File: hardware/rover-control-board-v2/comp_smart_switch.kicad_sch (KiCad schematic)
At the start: 26 parts, among them Q3 Q_NMOS_DGS, Q4 Q_PMOS_DGS, U2 BTH50015

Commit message: progress
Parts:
- added D12: RED, symbol Device:LED
- added J11: EXT_TEMP_PROBE, symbol Connector_Generic:Conn_01x02
- added Q2: Q_NMOS, symbol Device:Q_NMOS
- added R22, R24: 10k, symbol Device:R
- added R23: 100R, symbol Device:R
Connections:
- net GND: now also Q2.S, R24.2
- net 3V3: now reaches JP2.1 (A)
- net 3V3: now also JP1.1 (A), U1.2 (VCC), D12.2 (A)
- net TEMP_INT_: now reaches U1.11 (INT_)
- net SDATA: now reaches U1.12 (SDATA)
- net SCLK: now reaches U1.14 (SCLK)
- net TEMP_ALARM_: now reaches U1.16 (T_ALARM)
- net TEMP_ALARM_: now also R23.2
- net at U1.3 (D+): now also J11.2 (Pin_2)
- net at U1.4 (D-): now also J11.1 (Pin_1)
- new net: D12.1 (K), R22.2
- new net: Q2.D, R22.1
- new net: Q2.G, R23.1, R24.1
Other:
- note added: "1x02 pin header"
- note added: "OVER TEMP"
- note added: "Use 2N3906 for external temp probe"
- moved on the sheet: JP1, JP2

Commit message: Channels routed, temp bus pending
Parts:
- added C50: 100nF, symbol Device:C
- added D11, D13: ESD5Zxx, Diode_SMD:D_SOD-523, symbol Diode:ESD5Zxx
- J11: value EXT_TEMP_PROBE -> TEMP_PROBE
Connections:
- net 3V3: now also C50.2
- net GND: now also C50.1, D11.2 (A), D13.2 (A)
- net V_sense: now also D13.1 (K)
- net i_sense: now also D11.1 (K)
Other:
- note added: "5v varient needed"
- note removed: "Add TVS"
- note removed: "Add TVS or Opto Coupler"

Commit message: Bus routed
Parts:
- renumbered C50 to C16, C6 to C17, C2 to C18, C3 to C19, C4 to C20, C5 to C21, D3 to D5, D12 to D6, D11 to D7, D2 to D8, D13 to D9, J11 to J10, Q2 to Q5, R7 to R14, R5 to R15, R6 to R16, R2 to R18, R3 to R19, R4 to R20, R22 to R21, R23 to R22, R24 to R23, R8 to R24, R9 to R25, R11 to R26, R10 to R27, R12 to R28, R13 to R29, U1 to U5, U2 to U6

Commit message: revamping channel switches
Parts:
- renumbered C16 to C10, C17 to C11, C18 to C12, C19 to C13, C20 to C14, C21 to C15, J10 to J11, R14 to R13, R15 to R14, R16 to R15, R17 to R16, R18 to R17, R19 to R18, R20 to R19, R21 to R20, R22 to R21, R23 to R22, R24 to R23, R25 to R24, R26 to R25, R27 to R26, R28 to R27, R29 to R28, U5 to U4, U6 to U5
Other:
- moved on the sheet: C11, C12, C13, C14, C15, D7, D8, D9, R23, R24, R25, R26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

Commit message: 10v reg added for charge pumps
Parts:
- added Q25: CSD19533Q5A, Package_TO_SOT_SMD:TDSON-8-1, symbol Transistor_FET:CSD19533Q5A
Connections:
- new net: Q25.1 (S), Q25.2 (S), Q25.3 (S)
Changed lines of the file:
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@@
+	)
+	(symbol
+		(lib_id "Transistor_FET:CSD19533Q5A")
+		(at 149.86 106.68 0)
+		(unit 1)
+		(body_style 1)
+		(exclude_from_sim no)
+		(in_bom yes)
+		(on_board yes)
+		(in_pos_files yes)
+		(dnp no)
+		(fields_autoplaced yes)
+		(property "Reference" "Q25"
+			(at 156.21 105.4099 0)
+			(show_name no)
+			(do_not_autoplace no)
+			(effects
+				(font
+					(size 1.27 1.27)
+				)
+				(justify left)
+			)
+		)
+		(property "Value" "CSD19533Q5A"
+			(at 156.21 107.9499 0)
+			(show_name no)
+			(do_not_autoplace no)
+			(effects
+				(font
+					(size 1.27 1.27)
+				)
+				(justify left)
+			)
+		)
+		(property "Footprint" "Package_TO_SOT_SMD:TDSON-8-1"
+			(at 154.94 108.585 0)
+			(hide yes)
+			(show_name no)
+			(do_not_autoplace no)
+			(effects
+				(font
+					(size 1.27 1.27)
+					(italic yes)
+				)
+				(justify left)
+			)
+		)
+		(property "Datasheet" "http://www.ti.com/lit/gpn/csd19533q5a"
+			(at 154.94 110.49 0)
+			(hide yes)
+			(show_name no)
+			(do_not_autoplace no)
+			(effects
+				(font
+					(size 1.27 1.27)
+				)
+				(justify left)
+			)
+		)
+		(property "Description" "100A Id, 100V Vds, NexFET N-Channel Power MOSFET, 9.5mOhm Ron, 27nC Qg(typ), SON8 5x6mm"
+			(at 149.86 106.68 0)
+			(hide yes)
+			(show_name no)
+			(do_not_autoplace no)
+			(effects
+				(font
+					(size 1.27 1.27)
+				)
+			)
+		)
+		(pin "2"
+		)
+		(pin "4"
+		)
+		(pin "3"
+		)
+		(pin "1"
+		)
+		(pin "5"
+		)
+		(instances
+			(project "rover-control-board-v2"
+				(path "/ed12625f-743c-4dd1-a6f4-666aeca01e2d/977b49b6-52fe-4534-aa9a-ea79bcc5d2a2"
+					(reference "Q25")
+					(unit 1)
+				)
+			)
+		)
 	)
 	(symbol

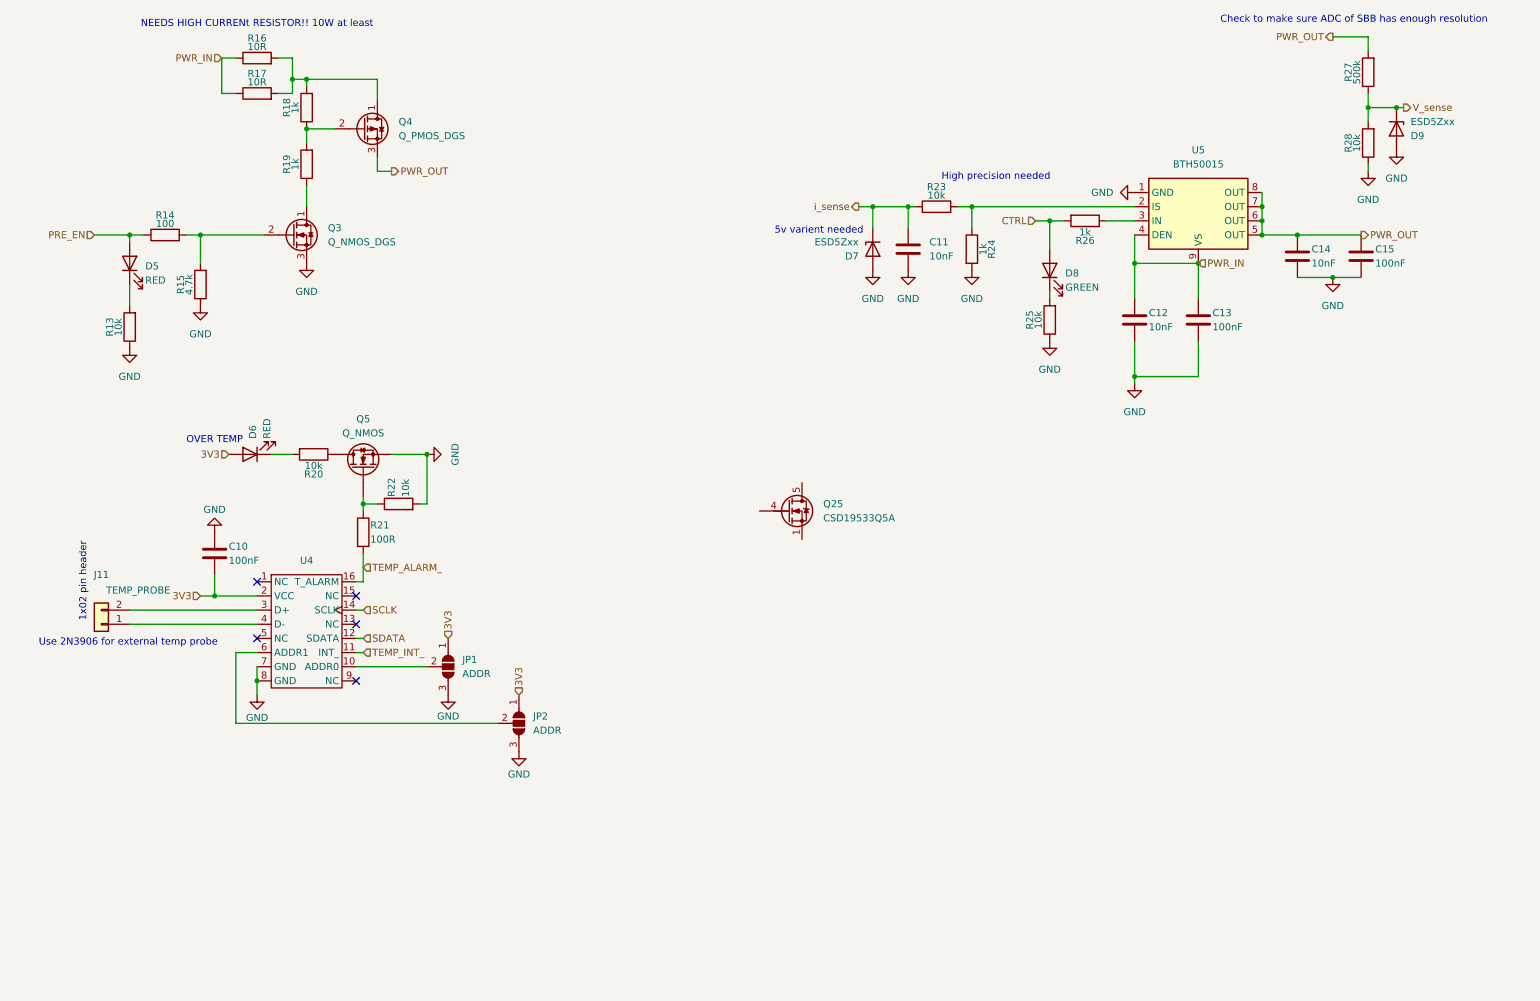
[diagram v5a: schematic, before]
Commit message: high power switch added
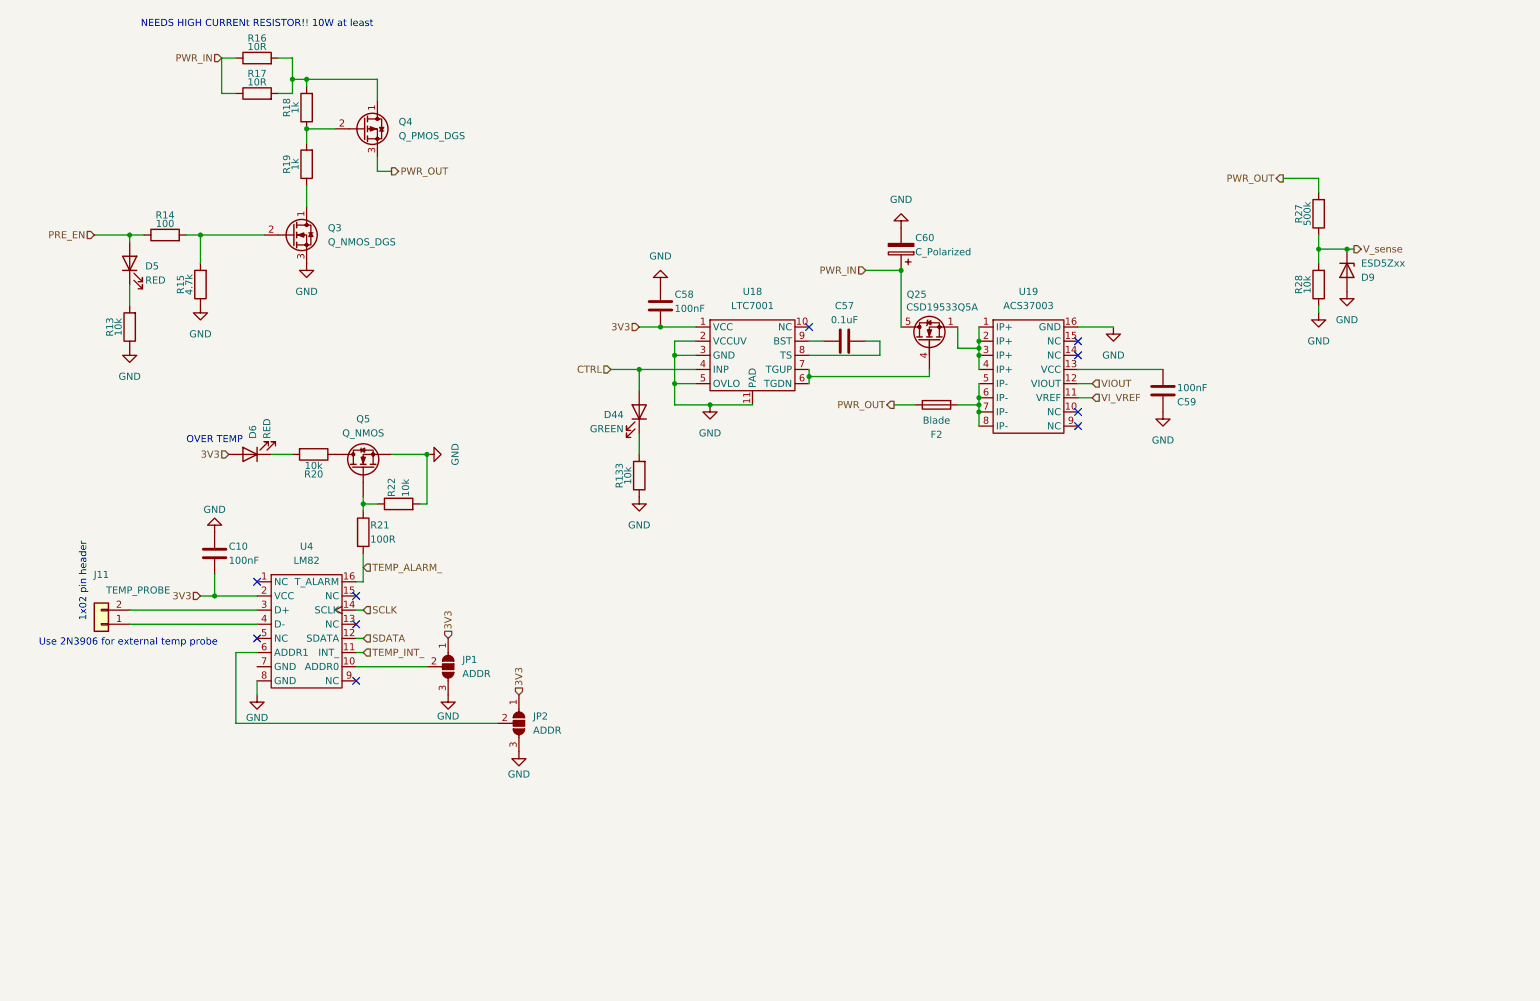
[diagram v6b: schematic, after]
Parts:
- removed C11, C12, C14: 10nF, symbol Device:C
- removed C13, C15: 100nF, symbol Device:C
- removed D7: ESD5Zxx, Diode_SMD:D_SOD-523, symbol Diode:ESD5Zxx
- removed D8: GREEN, symbol Device:LED
- removed R23, R25: 10k, symbol Device:R
- removed R24, R26: 1k, symbol Device:R
- removed U5: BTH50015, Package_SO:Infineon_PG-TSDSO-14-22, symbol component_library:BTH50015
- added C57: 0.1uF, symbol Device:C
- added C58, C59: 100nF, symbol Device:C
- added C60: C_Polarized, Capacitor_SMD:CP_Elec_10x10.5, symbol Device:C_Polarized
- added D44: GREEN, symbol Device:LED
- added F2: Blade, symbol Device:Fuse
- added R133: 10k, symbol Device:R
- added U18: LTC7001, Package_SO:MSOP-10-1EP_3x3mm_P0.5mm_EP1.68x1.88mm, symbol component_library:LTC7001
- added U19: ACS37003, Package_SO:SOIC-16W_7.5x10.3mm_P1.27mm, symbol component_library:ACS37003
- U4: value (none) -> LM82
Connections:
- net 3V3: now also C58.2, U18.1 (VCC)
- net CTRL: now also D44.2 (A), U18.4 (INP)
- net GND: now also C58.1, C59.1, C60.2, R133.1, U18.11 (PAD), U18.2 (VCCUV), U18.3 (GND), U18.5 (OVLO), U19.16 (GND); no longer U4.7 (GND)
- net PWR_IN: now also Q25.5 (D), C60.1
- net PWR_OUT: now also F2.1
- net at Q25.1 (S), Q25.2 (S), Q25.3 (S): now also U19.1 (IP+), U19.2 (IP+), U19.3 (IP+), U19.4 (IP+)
- net at Q25.4 (G): now also U18.6 (TGDN), U18.7 (TGUP)
- new net: C57.2, U18.8 (TS)
- new net: C57.1, U18.9 (BST)
- new net: C59.2, U19.13 (VCC)
- new net: F2.2, U19.5 (IP-), U19.6 (IP-), U19.7 (IP-), U19.8 (IP-)
- new net: D44.1 (K), R133.2
- new net VIOUT: U19.12 (VIOUT)
- new net VI_VREF: U19.11 (VREF)
- no-connect marks 5 -> 10
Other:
- note removed: "5v varient needed"
- note removed: "Check to make sure ADC of SBB has enough resolution"
- note removed: "High precision needed"
- moved on the sheet: D9, Q25, R27, R28

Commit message: Minor fixes and sanity checks
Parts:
- renumbered C10 to C14, C58 to C15, C57 to C16, C60 to C17, C59 to C18, D5 to D6, D6 to D7, D44 to D8, F2 to F1, J11 to J12, Q25 to Q6, R13 to R18, R14 to R19, R15 to R20, R16 to R21, R17 to R22, R18 to R23, R19 to R24, R20 to R25, R21 to R26, R22 to R27, R133 to R28, R27 to R29, R28 to R30, U18 to U5, U19 to U6
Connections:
- net 3V3: now also C18.2, U6.13 (VCC); no longer C15.2, U5.1 (VCC)
- net TEMP_INT_: no longer names the net of U4.11 (INT_)
- new net 10V: C15.2, U5.1 (VCC)
- no-connect marks 10 -> 11
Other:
- note added: "TODO: - Swap nmos to pmos for _T-ALARM - Sanity check charge pump config - Assign TVS diode"
- moved on the sheet: C15, C16, C17, C18, D8, D9, F1, Q6, R28, R29, R30, U5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
